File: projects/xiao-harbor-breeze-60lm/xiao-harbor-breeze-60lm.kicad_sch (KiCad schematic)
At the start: 17 parts, among them CN1 XY122V-5.08-2P, CN2 XY122V-5.08-2P, J1 1165SDIG-07, J2 1165SDIG-07, U1 BQ25185DLHR, U2 ME6210A33PG

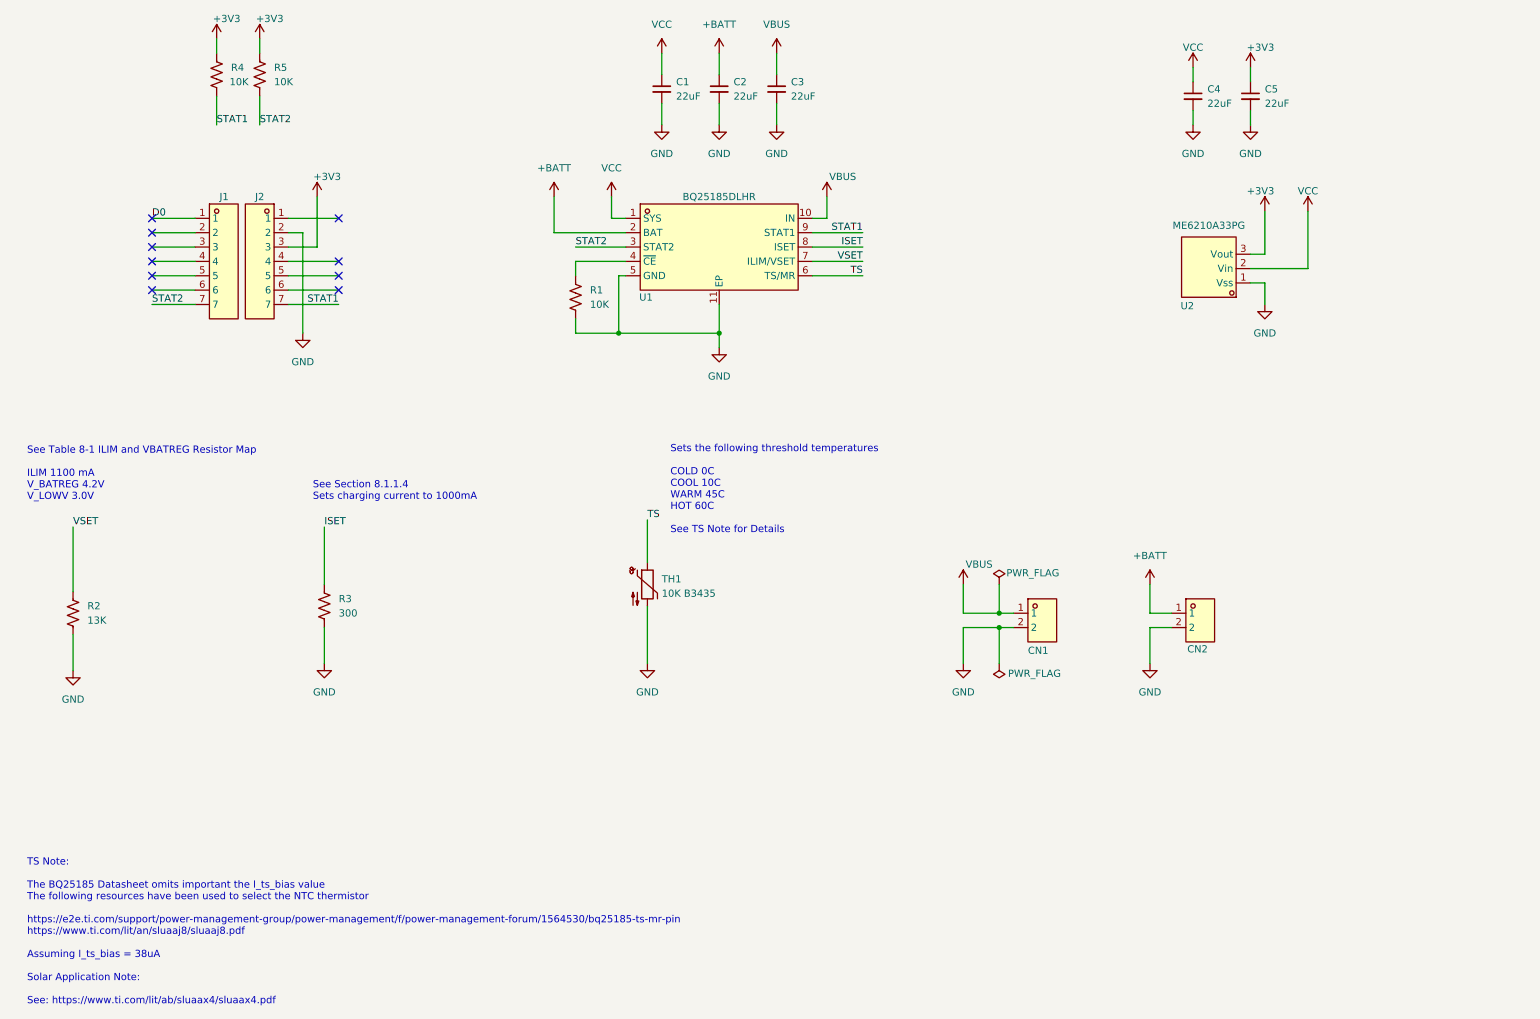
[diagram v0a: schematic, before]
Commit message: Add low voltage and over voltage protection
This part is a final safety net for battery charage management.

It is configured to have a low voltage cutoff of 2.5V and an over
voltage cutoff of 4.3V.

These values are comfortably outside the range of the change controller
thresholds, but still within the ranges generally accepted to avoid
permanent cell damage.

If for some reason we over charge or over discharge, this part will do a
low side disconnect of the battery from the rest of the system.

lib: Add simple logos

Currently unused, but are available.

See:
  * https://meshtastic.org/docs/legal/licensing-and-trademark/#community-project-logos-m-powered--m-pwrd
  * https://oshwa.org/resources/open-source-hardware-logo/
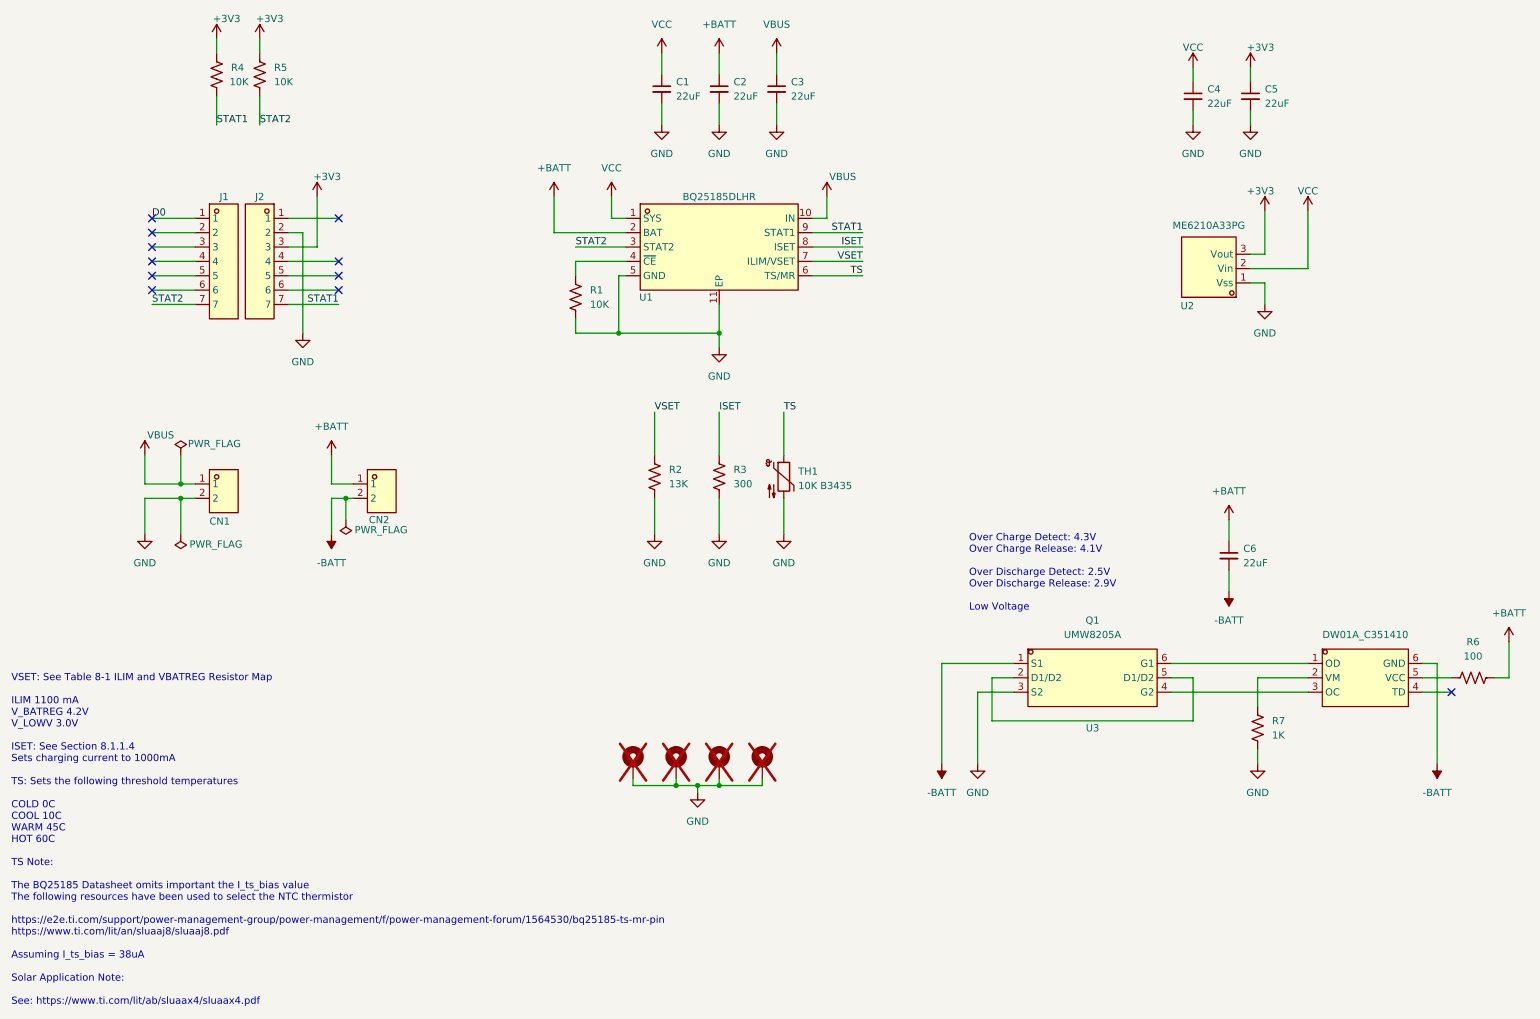
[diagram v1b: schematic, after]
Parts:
- added C6: 22uF, Capacitor_SMD:C_0805_2012Metric, symbol Device:C_Small
- added H1, H2, H3, H4: MountingHole_Pad, MountingHole:MountingHole_3.2mm_M3_ISO7380_Pad, symbol Mechanical:MountingHole_Pad
- added Q1: UMW8205A, easyeda2kicad:SOT-23-6_L2.9-W1.6-P0.95-LS2.8-BL, symbol easyeda2kicad:UMW8205A
- added R6: 100, Resistor_SMD:R_0603_1608Metric, symbol Device:R_US
- added R7: 1K, Resistor_SMD:R_0603_1608Metric, symbol Device:R_US
- added U3: DW01A_C351410, easyeda2kicad:SOT-23-6_L2.9-W1.6-P0.95-LS2.8-BL, symbol easyeda2kicad:DW01A_C351410
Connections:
- net +BATT: now also C6.1, R6.2
- net GND: now also H1.1, H2.1, H3.1, H4.1, Q1.3 (S2), R7.2; no longer CN2.2
- new net: R7.1, U3.2 (VM)
- new net: R6.1, U3.5 (VCC)
- new net: Q1.6 (G1), U3.1 (OD)
- new net: Q1.4 (G2), U3.3 (OC)
- new net: Q1.2 (D1/D2), Q1.5 (D1/D2)
- new net -BATT: C6.2, CN2.2, Q1.1 (S1), U3.6 (GND)
- no-connect marks 10 -> 11
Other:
- note added: "Over Charge Detect: 4.3V Over Charge Release: 4.1V Over Discharge Detect: 2.5V Over Discharge Release: 2.9V Low Voltage"
- note added: "VSET: See Table 8-1 ILIM and VBATREG Resistor Map ILIM 1100 mA V_BATREG 4.2V V_LOWV 3.0V ISET: See Section 8.1.1.4 Sets charging current to 1000mA TS: Sets the following threshold temperatures COLD 0C COOL 10C WARM 45C HOT 60C TS Note: The BQ25185 Datasheet omits important the I_ts_bias value The following resources have been used to select the NTC thermistor https://e2e.ti.com/support/power-mana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"
- note removed: "See Section 8.1.1.4 Sets charging current to 1000mA"
- note removed: "See Table 8-1 ILIM and VBATREG Resistor Map ILIM 1100 mA V_BATREG 4.2V V_LOWV 3.0V"
- note removed: "Sets the following threshold temperatures COLD 0C COOL 10C WARM 45C HOT 60C See TS Note for Details"
- note removed: "TS Note: The BQ25185 Datasheet omits important the I_ts_bias value The following resources have been used to select the NTC thermistor https://e2e.ti.com/support/power-management-group/power-management/f/power-management-forum/1564530/bq25185-ts-mr-pin https://www.ti.com/lit/an/sluaaj8/sluaaj8.pdf Assuming I_ts_bias = 38uA Solar Application Note: See: https://www.ti.com/lit/ab/sluaax4/sluaax4.pdf"
- title: (none) -> XIAO nRF52840 Harbor Breeze 60 Lumen Solar Meshtastic
- moved on the sheet: CN1, CN2, R2, R3, TH1

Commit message: Add ziptie mounting slots
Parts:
- Q1: JLCPCB PN (none) -> C351449
- R6: JLCPCB PN C23025 -> C22775
- R7: JLCPCB PN C23025 -> C21190
- U3: JLCPCB PN (none) -> C351410
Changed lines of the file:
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@@
 			)
 		)
-		(property "JLCPCB PN" "C23025"
+		(property "JLCPCB PN" "C21190"
 			(at 234.95 144.78 0)
 			(effects
@@
 			)
 		)
-		(property "JLCPCB PN" "C23025"
+		(property "JLCPCB PN" "C22775"
 			(at 273.05 135.89 0)
 			(effects
@@
 			)
 		)
+		(property "JLCPCB PN" "C351410"
+			(at 254 135.89 0)
+			(effects
+				(font
+					(size 1.27 1.27)
+				)
+				(hide yes)
+			)
+		)
 		(pin "4"
 		)
@@
 			(effects
 				(font
+					(size 1.27 1.27)
+				)
+				(hide yes)
+			)
+		)
+		(property "JLCPCB PN" "C351449"
+			(at 205.74 135.89 0)
+			(effects
+				(font

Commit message: Use horizontally oriented spring terminals
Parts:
- CN1, CN2: footprint easyeda2kicad:CONN-TH_XY122V-5.08-2P -> easyeda2kicad:CONN-TH_XY122R-5.08-2P; JLCPCB PN C784937 -> C784938; LCSC Part C784937 -> C784938
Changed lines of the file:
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@@
 			)
 		)
-		(property "Footprint" "easyeda2kicad:CONN-TH_XY122V-5.08-2P"
+		(property "Footprint" "easyeda2kicad:CONN-TH_XY122R-5.08-2P"
 			(at 52.07 111.76 0)
 			(effects
@@
 			)
 		)
-		(property "Datasheet" "https://lcsc.com/product-detail/Spring-Clamp-System-Terminal-Block_Ningbo-Xinlaiya-Elec-XY122V-5-08-2P_C784937.html"
+		(property "Datasheet" ""
 			(at 52.07 114.3 0)
 			(effects
@@
 			)
 		)
-		(property "LCSC Part" "C784937"
+		(property "LCSC Part" "C784938"
 			(at 52.07 116.84 0)
 			(effects
@@
 			)
 		)
-		(property "JLCPCB PN" "C784937"
+		(property "JLCPCB PN" "C784938"
 			(at 52.07 102.87 0)
 			(effects
@@
 			)
 		)
-		(property "Footprint" "easyeda2kicad:CONN-TH_XY122V-5.08-2P"
+		(property "Footprint" "easyeda2kicad:CONN-TH_XY122R-5.08-2P"
 			(at 80.01 111.76 0)
 			(effects
@@
 			)
 		)
-		(property "Datasheet" "https://lcsc.com/product-detail/Spring-Clamp-System-Terminal-Block_Ningbo-Xinlaiya-Elec-XY122V-5-08-2P_C784937.html"
+		(property "Datasheet" ""
 			(at 80.01 114.3 0)
 			(effects
@@
 			)
 		)
-		(property "LCSC Part" "C784937"
+		(property "LCSC Part" "C784938"
 			(at 80.01 116.84 0)
 			(effects
@@
 			)
 		)
-		(property "JLCPCB PN" "C784937"
+		(property "JLCPCB PN" "C784938"
 			(at 80.01 102.87 0)
 			(effects

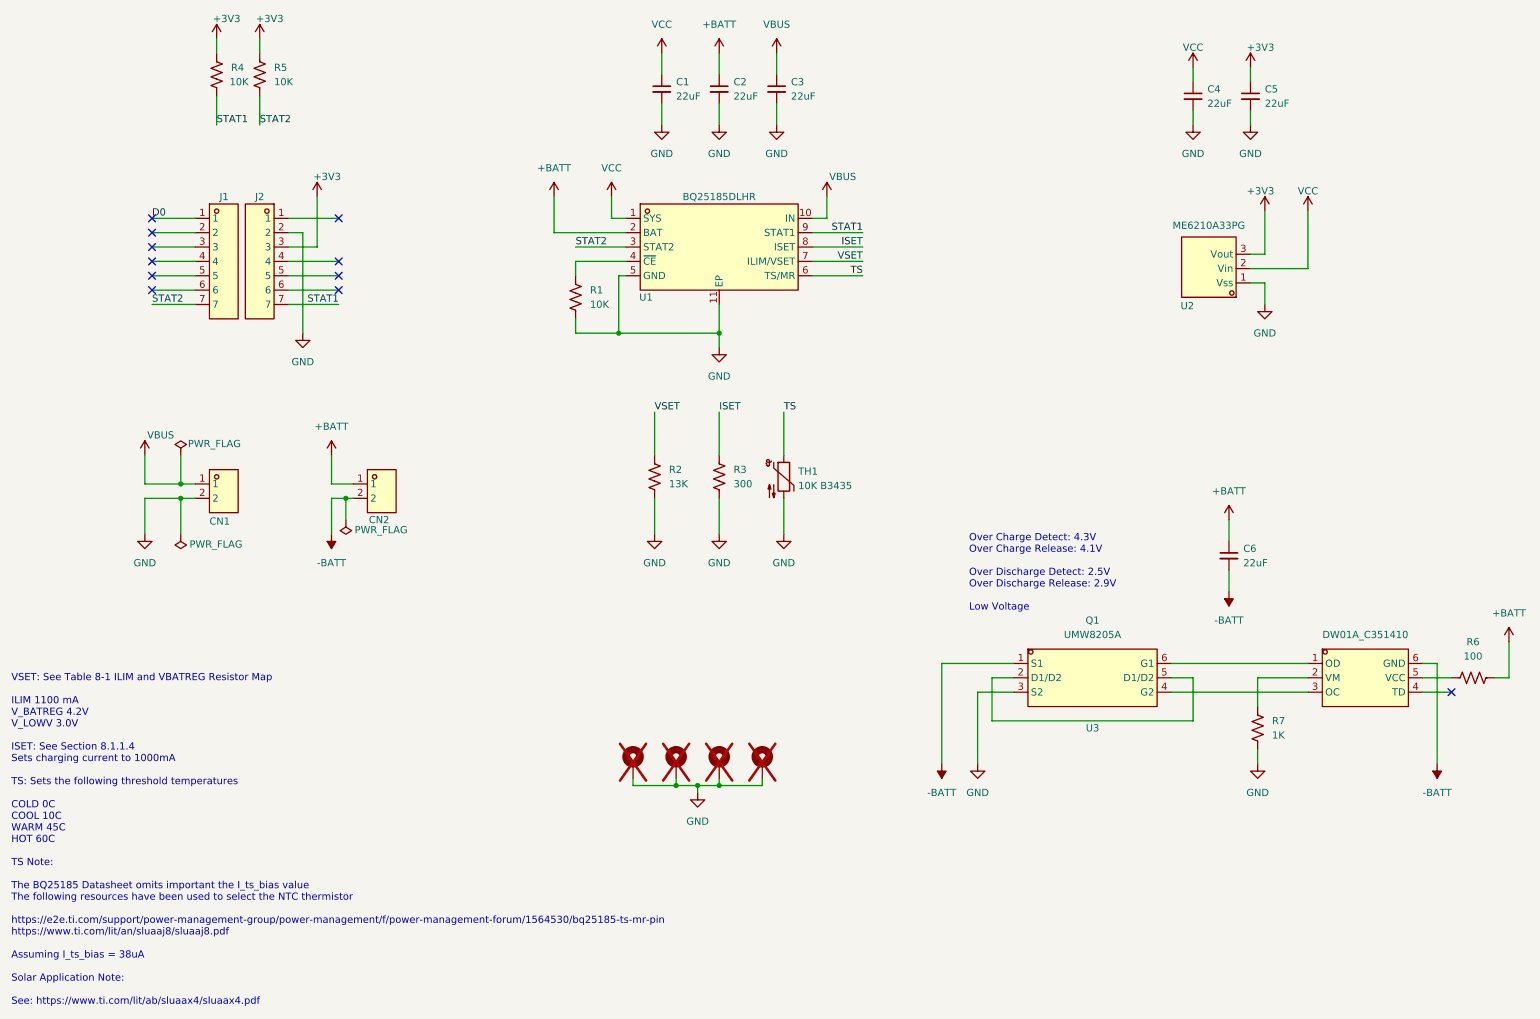
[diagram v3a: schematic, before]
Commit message: Add test points and status LEDs
LEDs allow simple confirmation of the board state. Cut their traces
after testing to save around 20mW of power draw.

Added test points to important signals to speed up diagnosing any issues
with the initial design.

Minor update to README.md
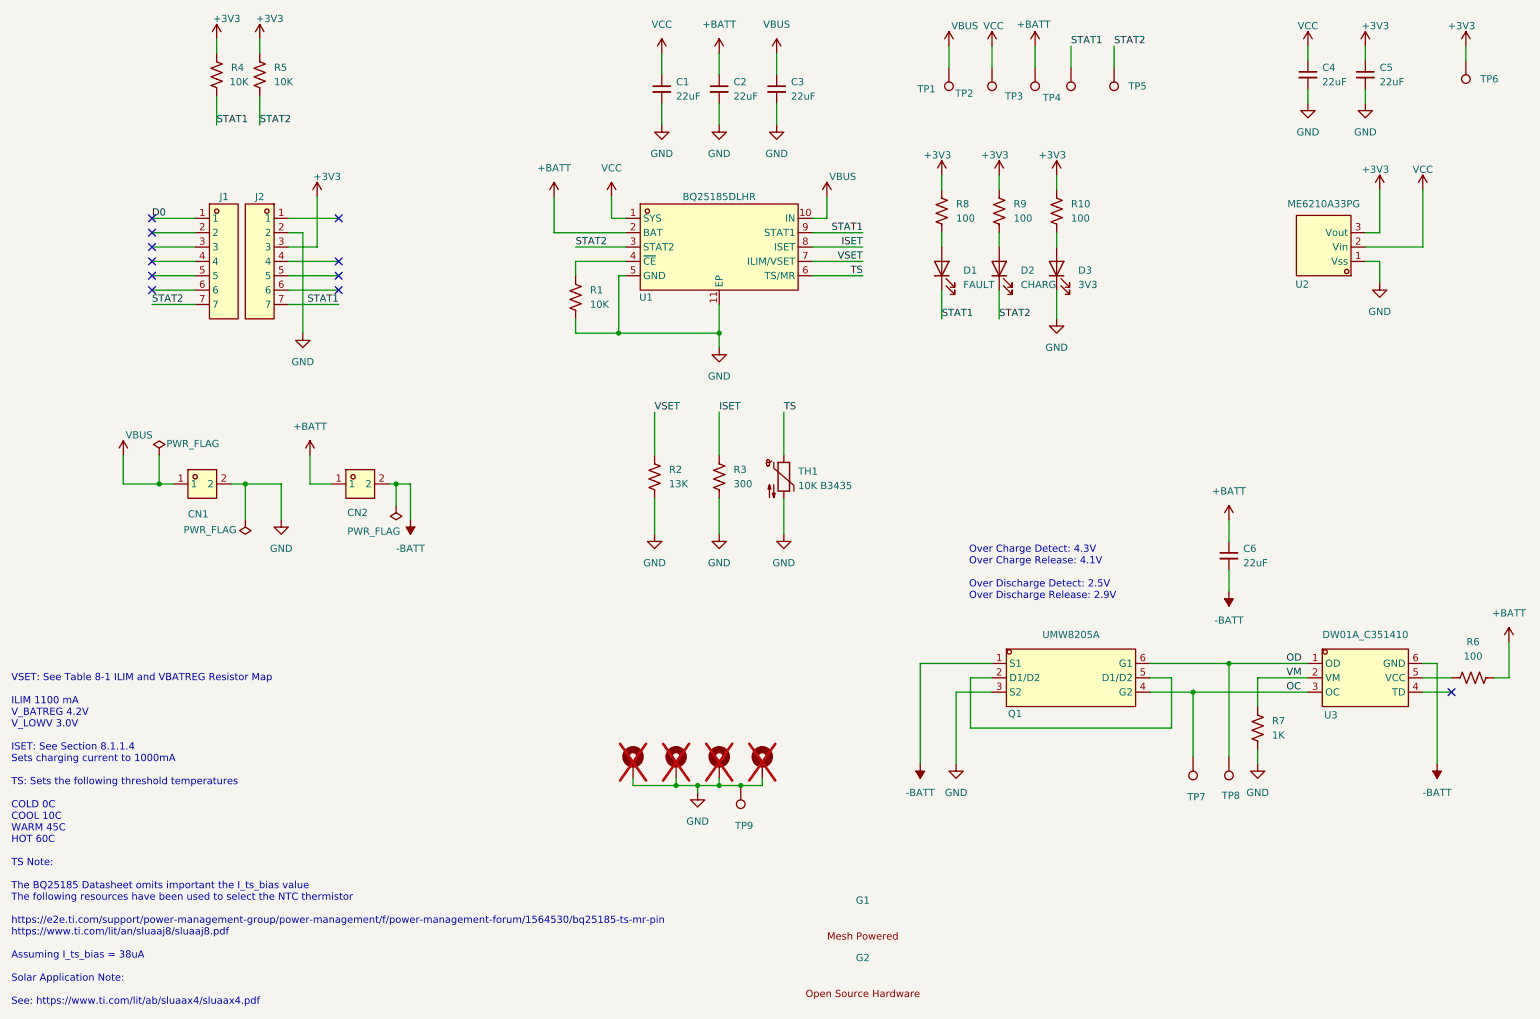
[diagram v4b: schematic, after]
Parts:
- added D1: FAULT, LED_SMD:LED_0603_1608Metric, symbol Device:LED
- added D2: CHARG, LED_SMD:LED_0603_1608Metric, symbol Device:LED
- added D3: 3V3, LED_SMD:LED_0603_1608Metric, symbol Device:LED
- added G1: ~, heliomesh:mesh_pwrd_very_small, symbol heliomesh:logo_mesh_pwrd
- added G2: ~, heliomesh:oshw_very_small, symbol heliomesh:logo_oshw
- added R10, R8, R9: 100, Resistor_SMD:R_0603_1608Metric, symbol Device:R_US
- added TP1, TP2, TP3, TP4, TP5, TP6, TP7, TP8, TP9: TestPoint, TestPoint:TestPoint_Pad_D1.5mm, symbol Connector:TestPoint
- CN1, CN2: value XY122V-5.08-2P -> XY122R-5.08-2P; symbol easyeda2kicad:XY122V-5.08-2P -> easyeda2kicad:XY122R-5.08-2P
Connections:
- net +3V3: now also R10.1, R8.1, R9.1, TP6.1
- net +BATT: now also TP3.1
- net GND: now also D3.1 (K), TP9.1
- net STAT1: now also D1.1 (K), TP4.1
- net STAT2: now also D2.1 (K), TP5.1
- net VBUS: now also TP1.1
- net VCC: now also TP2.1
- net VM: now reaches R7.1, U3.2 (VM)
- net OD: now reaches Q1.6 (G1), U3.1 (OD)
- net OD: now also TP8.1
- net OC: now reaches Q1.4 (G2), U3.3 (OC)
- net OC: now also TP7.1
- new net: D2.2 (A), R9.2
- new net: D1.2 (A), R8.2
- new net: D3.2 (A), R10.2
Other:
- note added: "Over Charge Detect: 4.3V Over Charge Release: 4.1V Over Discharge Detect: 2.5V Over Discharge Release: 2.9V"
- note removed: "Over Charge Detect: 4.3V Over Charge Release: 4.1V Over Discharge Detect: 2.5V Over Discharge Release: 2.9V Low Voltage"
- moved on the sheet: C4, C5, CN1, CN2, Q1, U2

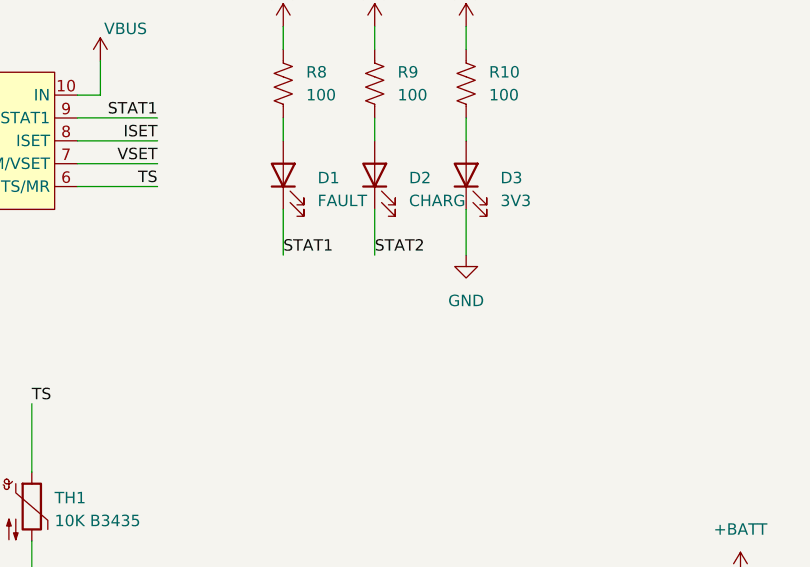
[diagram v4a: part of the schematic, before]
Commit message: Add user documented LED jumpers
Indicates to users that the LEDs are optional and documents how and
where to cut to conserve power.
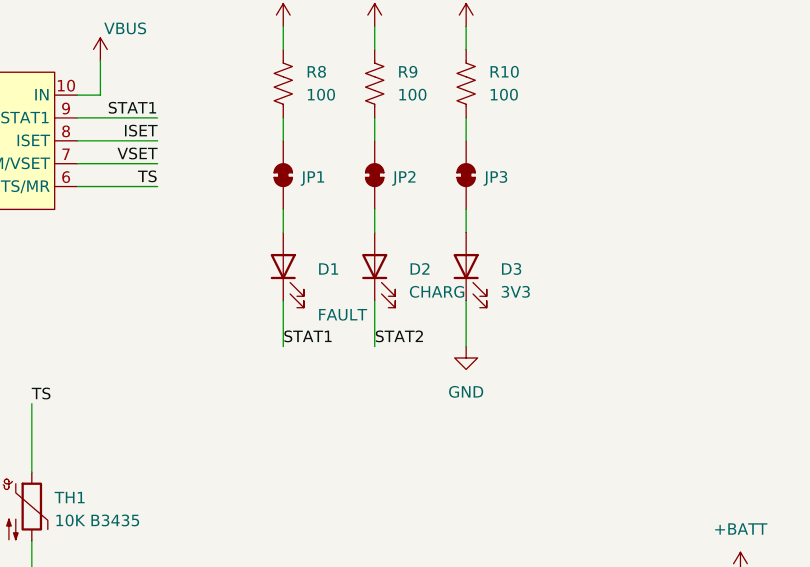
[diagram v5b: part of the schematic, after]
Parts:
- added JP1, JP2, JP3: SolderJumper_2_Bridged, Jumper:SolderJumper-2_P1.3mm_Bridged_RoundedPad1.0x1.5mm, symbol Jumper:SolderJumper_2_Bridged
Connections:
- net at R9.2: now also JP2.2 (B); no longer D2.2 (A)
- net at D1.2 (A): now also JP1.1 (A); no longer R8.2
- net at D3.2 (A): now also JP3.1 (A); no longer R10.2
- new net: D2.2 (A), JP2.1 (A)
- new net: JP3.2 (B), R10.2
- new net: JP1.2 (B), R8.2
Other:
- moved on the sheet: D1, D2, D3
